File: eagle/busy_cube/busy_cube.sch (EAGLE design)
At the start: 12 parts

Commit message: PCB changes
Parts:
- added EXT_SWITCH: (no value), busy_cube_lib:CONN_02-JST-2MM-SMT
- added R3: 300, busy_cube_lib:RESISTORAXIAL-0.3
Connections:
- new net N$10: BAT_CONN.1, EXT_SWITCH.2
- new net N$9: R3.2, SP1.+
- net BAT_IN_VCC: now also EXT_SWITCH.1; no longer BAT_CONN.1
- net SPKR: now also R3.1; no longer SP1.+
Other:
- moved on the sheet: SP1
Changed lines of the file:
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@@
 <part name="GND8" library="busy_cube_lib" deviceset="GND" device=""/>
 <part name="R2" library="busy_cube_lib" deviceset="RESISTOR" device="1206" value=" 0"/>
+<part name="R3" library="busy_cube_lib" deviceset="RESISTOR" device="AXIAL-0.3" value="300"/>
+<part name="EXT_SWITCH" library="busy_cube_lib" deviceset="CONN_02" device="-JST-2MM-SMT"/>
 </parts>
 <sheets>
@@
 <instance part="GND7" gate="1" x="111.76" y="38.1" rot="R180"/>
 <instance part="SUPPLY4" gate="G$1" x="111.76" y="22.86" rot="R180"/>
-<instance part="SP1" gate="S1" x="10.16" y="63.5" rot="R90"/>
-<instance part="GND8" gate="1" x="10.16" y="73.66" rot="R180"/>
+<instance part="SP1" gate="S1" x="7.62" y="63.5" rot="R90"/>
+<instance part="GND8" gate="1" x="7.62" y="73.66" rot="R180"/>
 <instance part="R2" gate="G$1" x="68.58" y="78.74"/>
+<instance part="R3" gate="G$1" x="15.24" y="58.42" rot="R180"/>
+<instance part="EXT_SWITCH" gate="G$1" x="73.66" y="114.3" rot="R90"/>
 </instances>
 <busses>
@@
 <segment>
 <pinref part="SP1" gate="S1" pin="-"/>
-<wire x1="10.16" y1="68.58" x2="10.16" y2="71.12" width="0.1524" layer="91"/>
+<wire x1="7.62" y1="68.58" x2="7.62" y2="71.12" width="0.1524" layer="91"/>
 <pinref part="GND8" gate="1" pin="GND"/>
 </segment>
@@
 <net name="BAT_IN_VCC" class="0">
 <segment>
-<pinref part="BAT_CONN" gate="G$1" pin="1"/>
-<wire x1="63.5" y1="124.46" x2="81.28" y2="124.46" width="0.1524" layer="91"/>
 <wire x1="81.28" y1="124.46" x2="81.28" y2="129.54" width="0.1524" layer="91"/>
 <pinref part="POWERBOOST" gate="G$1" pin="3VO"/>
 <wire x1="81.28" y1="129.54" x2="101.6" y2="129.54" width="0.1524" layer="91"/>
+<pinref part="EXT_SWITCH" gate="G$1" pin="1"/>
+<wire x1="73.66" y1="121.92" x2="73.66" y2="124.46" width="0.1524" layer="91"/>
+<wire x1="73.66" y1="124.46" x2="81.28" y2="124.46" width="0.1524" layer="91"/>
+<label x="78.74" y="129.54" size="1.778" layer="95"/>
 </segment>
 </net>
@@
 <segment>
 <pinref part="U$1" gate="G$1" pin="5"/>
-<pinref part="SP1" gate="S1" pin="+"/>
-<wire x1="33.02" y1="58.42" x2="10.16" y2="58.42" width="0.1524" layer="91"/>
+<wire x1="33.02" y1="58.42" x2="20.32" y2="58.42" width="0.1524" layer="91"/>
+<pinref part="R3" gate="G$1" pin="1"/>
 </segment>
 </net>
@@
 </segment>
 </net>
+<net name="N$9" class="0">
+<segment>
+<pinref part="SP1" gate="S1" pin="+"/>
+<pinref part="R3" gate="G$1" pin="2"/>
+<wire x1="10.16" y1="58.42" x2="7.62" y2="58.42" width="0.1524" layer="91"/>
+</segment>
+</net>
+<net name="N$10" class="0">
+<segment>
+<pinref part="BAT_CONN" gate="G$1" pin="1"/>
+<wire x1="63.5" y1="124.46" x2="71.12" y2="124.46" width="0.1524" layer="91"/>
+<pinref part="EXT_SWITCH" gate="G$1" pin="2"/>
+<wire x1="71.12" y1="124.46" x2="71.12" y2="121.92" width="0.1524" layer="91"/>
+</segment>
+</net>

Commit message: PCB changes
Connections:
- removed net N$7: S0.S, U$1.7
- new net N$11: S0.P, U$1.7
- net GND: now also S0.S; no longer S0.P
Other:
- moved on the sheet: S0
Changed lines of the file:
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@@
 <instance part="POWERBOOST" gate="G$1" x="104.14" y="124.46"/>
 <instance part="LIS3DH" gate="G$1" x="86.36" y="76.2" rot="MR180"/>
-<instance part="S0" gate="G$1" x="15.24" y="81.28" smashed="yes" rot="R270">
-<attribute name="NAME" x="13.335" y="85.725" size="1.778" layer="95"/>
+<instance part="S0" gate="G$1" x="15.24" y="83.82" smashed="yes" rot="R90">
+<attribute name="NAME" x="17.145" y="79.375" size="1.778" layer="95" rot="R180"/>
 </instance>
 <instance part="S1" gate="G$1" x="15.24" y="93.98" smashed="yes" rot="R270">
@@
 <wire x1="7.62" y1="91.44" x2="10.16" y2="91.44" width="0.1524" layer="91"/>
 <junction x="7.62" y="91.44"/>
-<wire x1="7.62" y1="91.44" x2="7.62" y2="78.74" width="0.1524" layer="91"/>
-<pinref part="S0" gate="G$1" pin="P"/>
-<wire x1="10.16" y1="78.74" x2="7.62" y2="78.74" width="0.1524" layer="91"/>
+<wire x1="7.62" y1="91.44" x2="7.62" y2="86.36" width="0.1524" layer="91"/>
+<pinref part="S0" gate="G$1" pin="S"/>
+<wire x1="10.16" y1="86.36" x2="7.62" y2="86.36" width="0.1524" layer="91"/>
 </segment>
 <segment>
@@
 <net name="N$7" class="0">
 <segment>
-<pinref part="S0" gate="G$1" pin="S"/>
-<wire x1="20.32" y1="78.74" x2="22.86" y2="78.74" width="0.1524" layer="91"/>
 <wire x1="22.86" y1="78.74" x2="22.86" y2="63.5" width="0.1524" layer="91"/>
-<pinref part="U$1" gate="G$1" pin="7"/>
-<wire x1="22.86" y1="63.5" x2="33.02" y2="63.5" width="0.1524" layer="91"/>
 </segment>
 </net>
@@
 </segment>
 </net>
+<net name="N$11" class="0">
+<segment>
+<pinref part="S0" gate="G$1" pin="P"/>
+<wire x1="20.32" y1="86.36" x2="20.32" y2="63.5" width="0.1524" layer="91"/>
+<pinref part="U$1" gate="G$1" pin="7"/>
+<wire x1="20.32" y1="63.5" x2="33.02" y2="63.5" width="0.1524" layer="91"/>
+</segment>
+</net>

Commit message: Code used in first version of the box
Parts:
- R1: value 500 -> 470
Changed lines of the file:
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@@
 <part name="BAT_CONN" library="busy_cube_lib" deviceset="CONN_02" device="-JST-2MM-SMT"/>
 <part name="NEO_PIXELS" library="busy_cube_lib" deviceset="CONN_03" device="LONGPADS"/>
-<part name="R1" library="busy_cube_lib" deviceset="RESISTOR" device="AXIAL-0.3" value=" 500"/>
+<part name="R1" library="busy_cube_lib" deviceset="RESISTOR" device="AXIAL-0.3" value="470"/>
 <part name="GND1" library="busy_cube_lib" deviceset="GND" device=""/>
 <part name="SUPPLY1" library="busy_cube_lib" deviceset="VCC" device=""/>

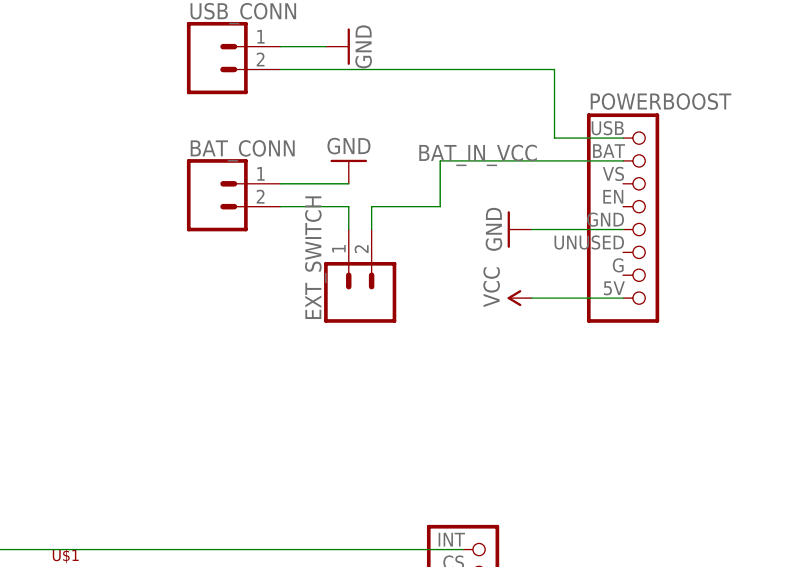
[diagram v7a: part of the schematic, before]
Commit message: Switch is now connected to the EN pin
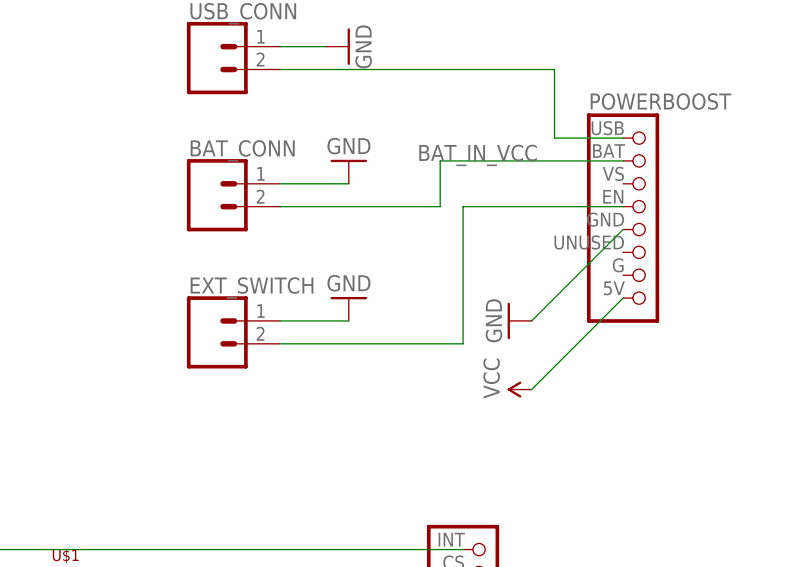
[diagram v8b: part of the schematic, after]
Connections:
- net BAT_IN_VCC: now also BAT_CONN.1; no longer EXT_SWITCH.1
- net GND: now also EXT_SWITCH.2
- net N$10: now also EXT_SWITCH.1, POWERBOOST.SCL; no longer BAT_CONN.1, EXT_SWITCH.2
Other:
- moved on the sheet: EXT_SWITCH
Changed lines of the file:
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@@
 <?xml version="1.0" encoding="utf-8"?>
 <!DOCTYPE eagle SYSTEM "eagle.dtd">
-<eagle version="8.3.2">
+<eagle version="8.5.2">
 <drawing>
 <settings>
@@
 <part name="R3" library="busy_cube_lib" deviceset="RESISTOR" device="AXIAL-0.3" value="300"/>
 <part name="EXT_SWITCH" library="busy_cube_lib" deviceset="CONN_02" device="-JST-2MM-SMT"/>
+<part name="GND9" library="busy_cube_lib" deviceset="GND" device=""/>
 </parts>
 <sheets>
@@
 <instance part="NEO_PIXELS" gate="J$1" x="124.46" y="30.48" rot="R180"/>
 <instance part="R1" gate="G$1" x="93.98" y="35.56" rot="R90"/>
-<instance part="GND1" gate="1" x="88.9" y="121.92" rot="R270"/>
-<instance part="SUPPLY1" gate="G$1" x="91.44" y="114.3" rot="R90"/>
+<instance part="GND1" gate="1" x="88.9" y="111.76" rot="R270"/>
+<instance part="SUPPLY1" gate="G$1" x="91.44" y="104.14" rot="R90"/>
 <instance part="GND2" gate="1" x="78.74" y="48.26" rot="R90"/>
 <instance part="SUPPLY2" gate="G$1" x="68.58" y="45.72" rot="R270"/>
@@
 <instance part="R2" gate="G$1" x="68.58" y="78.74"/>
 <instance part="R3" gate="G$1" x="15.24" y="58.42" rot="R180"/>
-<instance part="EXT_SWITCH" gate="G$1" x="73.66" y="114.3" rot="R90"/>
+<instance part="EXT_SWITCH" gate="G$1" x="55.88" y="109.22"/>
+<instance part="GND9" gate="1" x="71.12" y="114.3" rot="R180"/>
 </instances>
 <busses>
@@
 <segment>
 <pinref part="POWERBOOST" gate="G$1" pin="SDA"/>
-<wire x1="101.6" y1="121.92" x2="91.44" y2="121.92" width="0.1524" layer="91"/>
+<wire x1="101.6" y1="121.92" x2="91.44" y2="111.76" width="0.1524" layer="91"/>
 <pinref part="GND1" gate="1" pin="GND"/>
 </segment>
@@
 <pinref part="GND8" gate="1" pin="GND"/>
 </segment>
+<segment>
+<pinref part="EXT_SWITCH" gate="G$1" pin="2"/>
+<pinref part="GND9" gate="1" pin="GND"/>
+<wire x1="63.5" y1="111.76" x2="71.12" y2="111.76" width="0.1524" layer="91"/>
+</segment>
 </net>
 <net name="VCC" class="0">
 <segment>
 <pinref part="POWERBOOST" gate="G$1" pin="INT"/>
-<wire x1="101.6" y1="114.3" x2="91.44" y2="114.3" width="0.1524" layer="91"/>
+<wire x1="101.6" y1="114.3" x2="91.44" y2="104.14" width="0.1524" layer="91"/>
 <pinref part="SUPPLY1" gate="G$1" pin="VCC"/>
 </segment>
@@
 <pinref part="POWERBOOST" gate="G$1" pin="3VO"/>
 <wire x1="81.28" y1="129.54" x2="101.6" y2="129.54" width="0.1524" layer="91"/>
-<pinref part="EXT_SWITCH" gate="G$1" pin="1"/>
-<wire x1="73.66" y1="121.92" x2="73.66" y2="124.46" width="0.1524" layer="91"/>
-<wire x1="73.66" y1="124.46" x2="81.28" y2="124.46" width="0.1524" layer="91"/>
 <label x="78.74" y="129.54" size="1.778" layer="95"/>
+<pinref part="BAT_CONN" gate="G$1" pin="1"/>
+<wire x1="81.28" y1="124.46" x2="63.5" y2="124.46" width="0.1524" layer="91"/>
 </segment>
 </net>
@@
 </segment>
 </net>
-<net name="N$10" class="0">
-<segment>
-<pinref part="BAT_CONN" gate="G$1" pin="1"/>
-<wire x1="63.5" y1="124.46" x2="71.12" y2="124.46" width="0.1524" layer="91"/>
-<pinref part="EXT_SWITCH" gate="G$1" pin="2"/>
-<wire x1="71.12" y1="124.46" x2="71.12" y2="121.92" width="0.1524" layer="91"/>
-</segment>
-</net>
 <net name="N$11" class="0">
 <segment>
@@
 </segment>
 </net>
+<net name="N$10" class="0">
+<segment>
+<pinref part="POWERBOOST" gate="G$1" pin="SCL"/>
+<wire x1="101.6" y1="124.46" x2="83.82" y2="124.46" width="0.1524" layer="91"/>
+<wire x1="83.82" y1="124.46" x2="83.82" y2="109.22" width="0.1524" layer="91"/>
+<pinref part="EXT_SWITCH" gate="G$1" pin="1"/>
+<wire x1="63.5" y1="109.22" x2="83.82" y2="109.22" width="0.1524" layer="91"/>
+</segment>
+</net>
